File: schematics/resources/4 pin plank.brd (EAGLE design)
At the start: 80 x 49 mm, 18 parts, among them IC1 74AHC1G86DBV

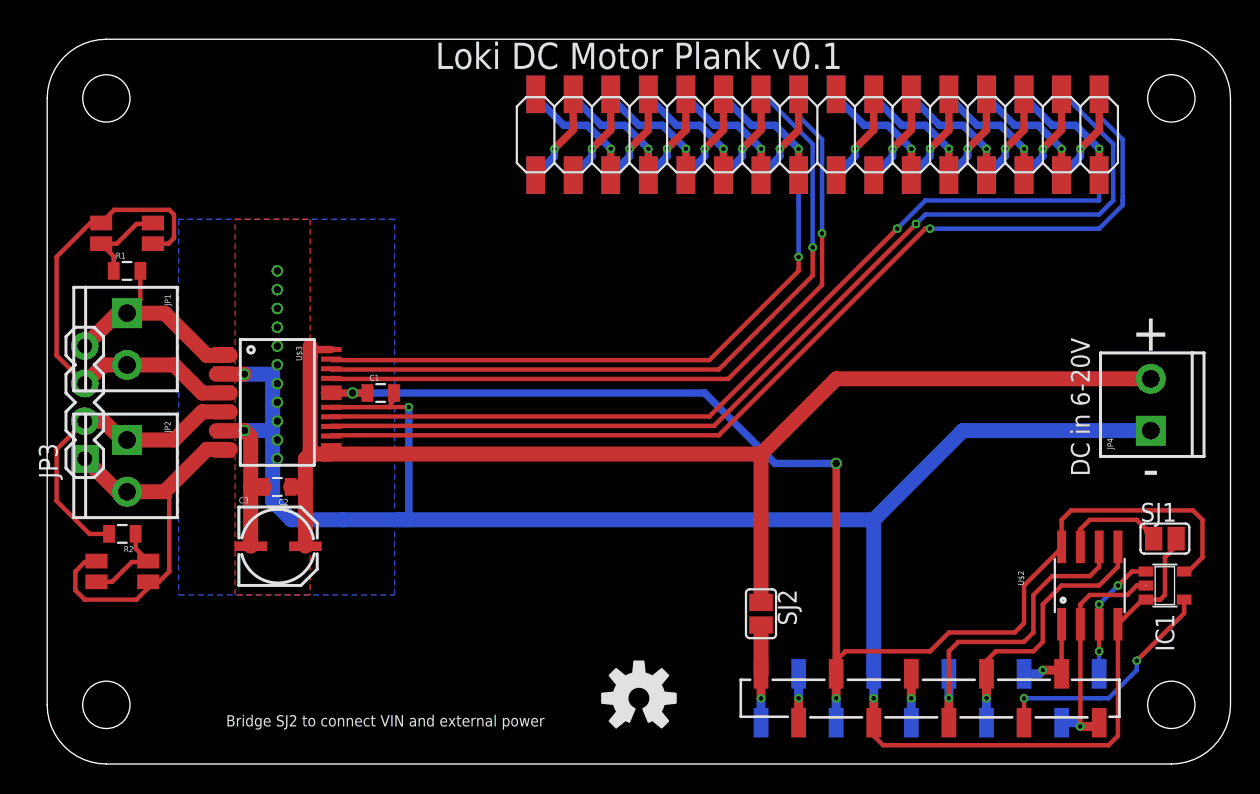
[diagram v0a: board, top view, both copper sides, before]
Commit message: Tweaks to planks; change 0604 parts for 0805 where possible
Also added 4 pin plank; minor text changes.
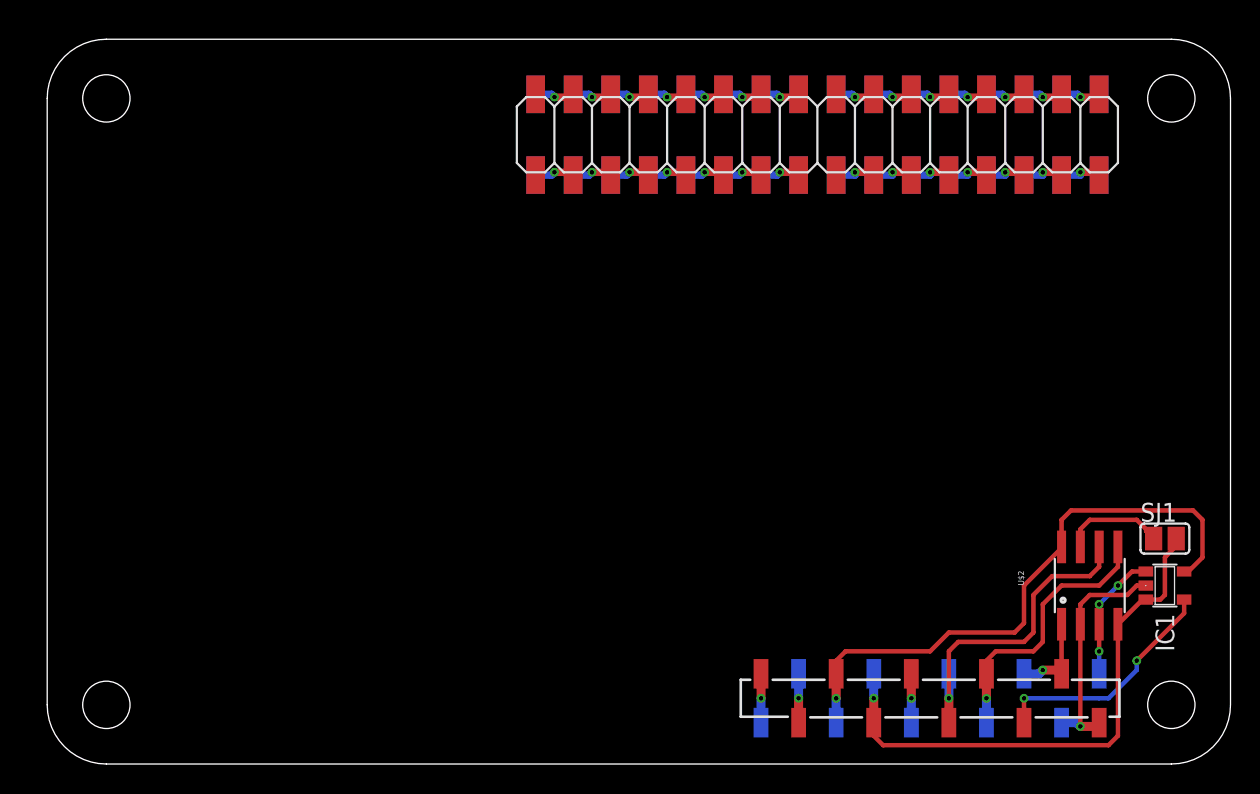
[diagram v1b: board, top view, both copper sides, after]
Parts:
- removed C1, C2: 0.1u, SparkFun-Passives:0805
- removed C3: 10u, SparkFun-Passives:PANASONIC_C
- removed JP1, JP2, JP4: (no value), SparkFun-Connectors:SCREWTERMINAL-3.5MM-2
- removed JP3: (no value), SparkFun-Connectors:1X04
- removed R1, R2: (no value), SparkFun-Passives:0805
- removed SJ2: (no value), jumper:SJ
- removed U$3: TB6621FNG, SparkFun-PowerIC:SSOP24
- removed U$4: (no value), SparkFun-Aesthetics:OSHW-LOGO-M
- removed U$5, U$6: BILED, nickparts:BILED
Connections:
- removed net AIN1: U$1.I2.1, U$3.21
- removed net AIN2: U$1.I2.3, U$3.22
- removed net BIN1: U$1.I1.2, U$3.17
- removed net BIN2: U$1.I1.3, U$3.16
- removed net N$29: JP1.1, JP3.4, R1.2, U$3.1, U$3.2
- removed net N$33: R1.1, U$5.A2, U$5.C1
- removed net N$34: R2.1, U$6.A2, U$6.C1
- removed net N$35: JP1.2, JP3.3, U$3.5, U$3.6, U$5.A1, U$5.C2
- removed net N$36: JP2.2, JP3.1, U$3.11, U$3.12, U$6.A1, U$6.C2
- removed net PWMA: U$1.I2.2, U$3.23
- removed net PWMB: U$1.I1.1, U$3.15
- removed net VMOT: C2.1, C3.+, JP4.2, SJ2.1, U$3.13, U$3.14, U$3.24
- new net N$28: U$1.I2.3, U$1.O2.1
- net +3V3: no longer C1.1, U$3.19, U$3.20
- net GND: no longer C1.2, C2.2, C3.-, JP4.1, U$3.10, U$3.18, U$3.3, U$3.4, U$3.9
- net N$1: now also U$1.O1.14; no longer U$1.O1.13
- net N$10: now also U$1.O1.5; no longer U$1.O1.4
- net N$11: now also U$1.O1.4; no longer U$1.O1.3
- net N$12: now also U$1.O1.3; no longer U$1.O1.2
- net N$13: now also U$1.O1.2; no longer U$1.O1.1
- net N$14: now also U$1.I1.3, U$1.O1.1; no longer U$1.I2.16, U$1.O2.13
- net N$15: now also U$1.I2.16, U$1.O2.14; no longer U$1.I2.15, U$1.O2.12
- net N$16: now also U$1.I2.15, U$1.O2.13; no longer U$1.I2.14, U$1.O2.11
- net N$17: now also U$1.I2.14, U$1.O2.12; no longer U$1.I2.13, U$1.O2.10
- net N$18: now also U$1.I2.13, U$1.O2.11; no longer U$1.I2.12, U$1.O2.9
- net N$19: now also U$1.I2.12, U$1.O2.10; no longer U$1.I2.11, U$1.O2.8
- net N$2: now also U$1.O1.13; no longer U$1.O1.12
- net N$20: now also U$1.I2.11, U$1.O2.9; no longer U$1.I2.10, U$1.O2.7
- net N$21: now also U$1.I2.10, U$1.O2.8; no longer U$1.I2.9, U$1.O2.6
- net N$22: now also U$1.I2.9, U$1.O2.7; no longer U$1.I2.8, U$1.O2.5
- net N$23: now also U$1.I2.8, U$1.O2.6; no longer U$1.I2.7, U$1.O2.4
- net N$24: now also U$1.I2.7, U$1.O2.5; no longer U$1.I2.6, U$1.O2.3
- net N$25: now also U$1.I2.6, U$1.O2.4; no longer U$1.I2.5, U$1.O2.2
- net N$26: now also U$1.I2.5, U$1.O2.3; no longer U$1.I2.4, U$1.O2.1
- net N$27: now also U$1.I2.4, U$1.O2.2; no longer JP2.1, JP3.2, R2.2, U$3.7, U$3.8
- net N$3: now also U$1.O1.12; no longer U$1.O1.11
- net N$4: now also U$1.O1.11; no longer U$1.O1.10
- net N$5: now also U$1.O1.10; no longer U$1.O1.9
- net N$6: now also U$1.O1.9; no longer U$1.O1.8
- net N$7: now also U$1.O1.8; no longer U$1.O1.7
- net N$8: now also U$1.O1.7; no longer U$1.O1.6
- net N$9: now also U$1.O1.6; no longer U$1.O1.5
- net V+: no longer SJ2.2
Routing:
- net GND: track 152.1 -> 36.9 mm, vias 15 -> 1
- net VMOT: track 86.1 -> 0.00 mm
- net PWMB: track 68.1 -> 0.00 mm, vias 1 -> 0
- net BIN2: track 67.9 -> 0.00 mm, vias 1 -> 0
- net BIN1: track 59.7 -> 0.00 mm, vias 1 -> 0
- net +3V3: track 92.1 -> 40.2 mm, vias 3 -> 1
- net AIN1: track 49.4 -> 0.00 mm, vias 1 -> 0
- net AIN2: track 49.0 -> 0.00 mm, vias 1 -> 0
- net PWMA: track 40.6 -> 0.00 mm, vias 1 -> 0
- net N$35: track 34.2 -> 0.00 mm
- net N$36: track 29.3 -> 0.00 mm
- net N$27: track 23.0 -> 2.70 mm, vias 0 -> 1
- net N$29: track 16.5 -> 0.00 mm
- net N$33: track 6.27 -> 0.00 mm
- net N$34: track 6.27 -> 0.00 mm
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- removed copper zone on layer 1, net GND
- removed copper zone on layer 16, net GND
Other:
- board text removed: "+"
- board text removed: "-"
- board text removed: "Bridge SJ2 to connect VIN and external power"
- board text removed: "DC in 6-20V"
- board text removed: "Loki DC Motor Plank v0.1"
